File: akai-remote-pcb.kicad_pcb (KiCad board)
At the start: 2 copper layers, 55 x 35 mm, 19 parts, among them J1 Conn_01x11, Q1 T2N7002AK, Q2 T2N7002AK, Q3 T2N7002AK, Q4 T2N7002AK, Q5 T2N7002AK, Q6 T2N7002AK, Q7 T2N7002AK, U1 MOUDLE-SEEEDUINO-XIAO-ESP32C3

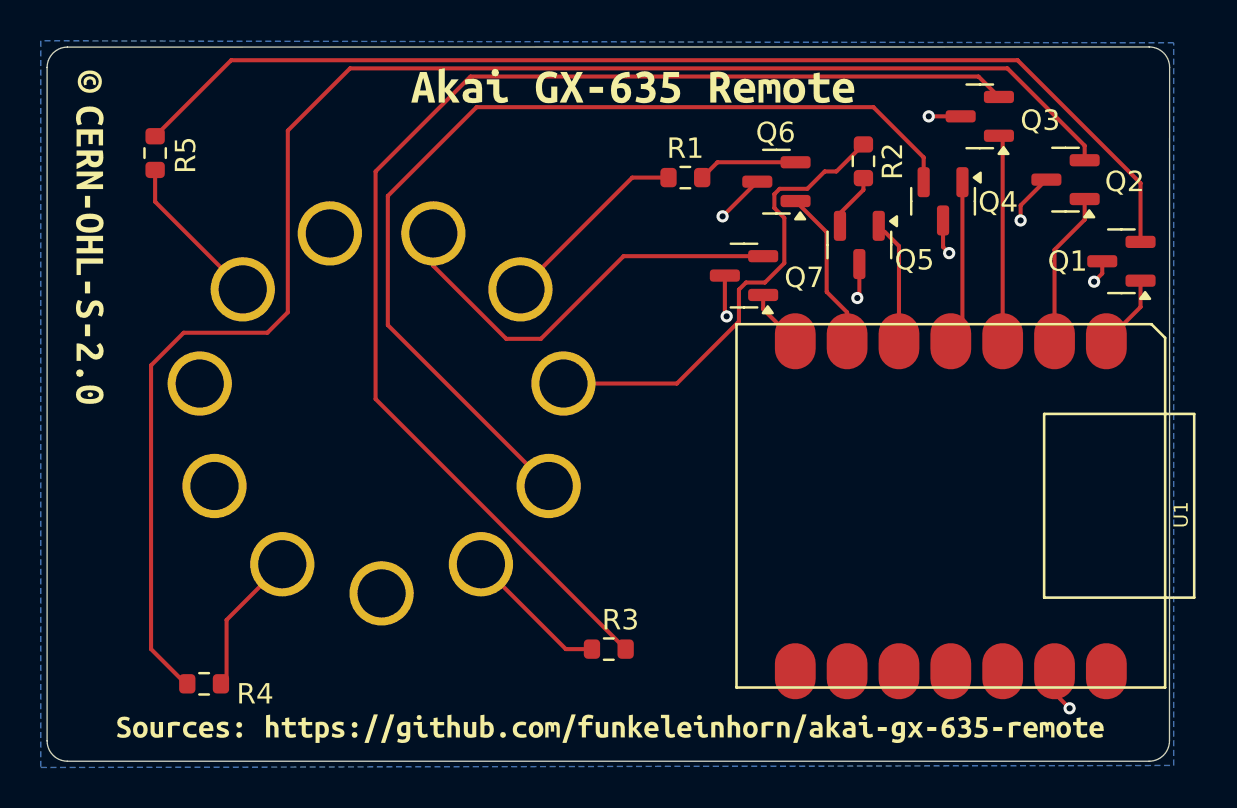
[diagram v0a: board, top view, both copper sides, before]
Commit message: Fix MOSFET direction and add external pull-down resistors
This commit fixes the direction of the MOSFETs and adds external
pull-down resistors to their gates to prevent undefined behavior when
the ESP is not powered.
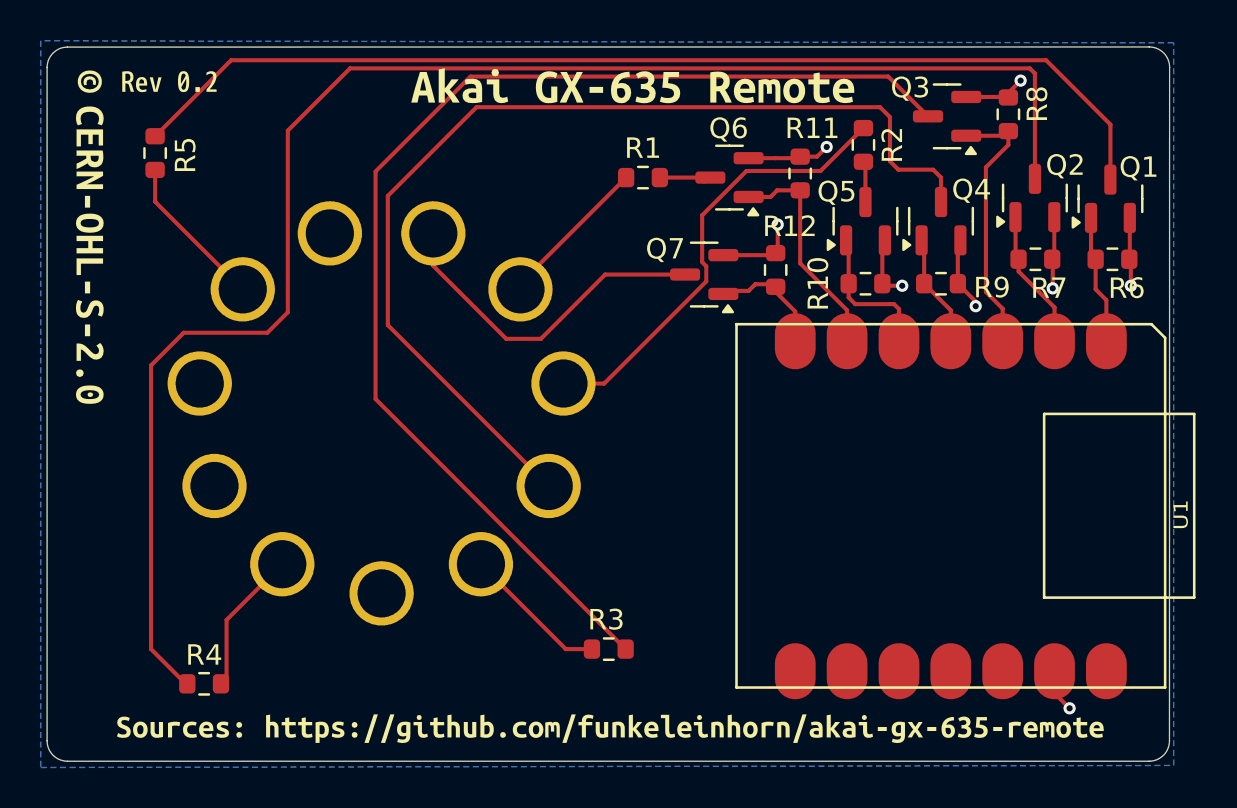
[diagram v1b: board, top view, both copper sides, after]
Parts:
- added R10: 100K, Resistor_SMD:R_0603_1608Metric, F.Cu at (162.3, 90.1)
- added R11: 100K, Resistor_SMD:R_0603_1608Metric, F.Cu at (159.1, 84.7)
- added R12: 100K, Resistor_SMD:R_0603_1608Metric, F.Cu at (157.9, 89.4)
- added R6: 100K, Resistor_SMD:R_0603_1608Metric, F.Cu at (174.4, 88.9)
- added R7: 100K, Resistor_SMD:R_0603_1608Metric, F.Cu at (170.6, 88.9)
- added R8: 100K, Resistor_SMD:R_0603_1608Metric, F.Cu at (169.3, 81.8)
- added R9: 100K, Resistor_SMD:R_0603_1608Metric, F.Cu at (166.0, 90.1)
- added kibuzzard-68C59956: G***, kibuzzard-68C59956, F.Cu at (128.2, 80.2)
- moved Q1 3.11 mm to (174.3, 85.9), turned to 90 degrees
- moved Q6 2.31 mm to (155.6, 84.9)
- moved R1 2.07 mm to (151.4, 84.9)
- moved Q7 1.95 mm to (154.4, 89.7)
- moved Q2 1.75 mm to (170.6, 85.9), turned to 90 degrees
- moved Q3 1.60 mm to (166.3, 81.9)
- moved Q5 1.20 mm to (162.3, 87.0), turned to 90 degrees
- moved Q4 0.98 mm to (166.0, 87.0), turned to 90 degrees
- moved R2 0.80 mm to (162.2, 83.3)
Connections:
- Q1 pad 2: Net-(Q1-S) -> GND
- Q1 pad 3: GND -> Net-(Q1-D)
- Q2 pad 2: Net-(Q2-S) -> GND
- Q2 pad 3: GND -> Net-(Q2-D)
- Q3 pad 2: Net-(Q3-S) -> GND
- Q3 pad 3: GND -> Net-(Q3-D)
- Q4 pad 2: /RWD -> GND
- Q4 pad 3: GND -> /RWD
- Q5 pad 2: Net-(Q5-S) -> GND
- Q5 pad 3: GND -> Net-(Q5-D)
- Q6 pad 2: Net-(Q6-S) -> GND
- Q6 pad 3: GND -> Net-(Q6-D)
- Q7 pad 2: /FF -> GND
- Q7 pad 3: GND -> /FF
- R1 pad 2: Net-(Q6-S) -> Net-(Q6-D)
- R2 pad 2: Net-(Q5-S) -> Net-(Q5-D)
- R3 pad 2: Net-(Q3-S) -> Net-(Q3-D)
- R4 pad 2: Net-(Q2-S) -> Net-(Q2-D)
- R5 pad 2: Net-(Q1-S) -> Net-(Q1-D)
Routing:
- net Net-(Q2-D): track 0.00 -> 76.2 mm
- net Net-(Q2-S): track 75.6 -> 0.00 mm
- net Net-(Q3-S): track 61.4 -> 0.00 mm
- net Net-(Q3-D): track 0.00 -> 58.3 mm
- net Net-(Q1-S): track 55.2 -> 0.00 mm
- net Net-(Q1-D): track 0.00 -> 52.3 mm
- net GND: track 15.0 -> 27.4 mm
- net Net-(Q6-S): track 4.89 -> 0.00 mm
- net /FF: track 20.9 -> 16.7 mm
- net Net-(Q6-G): track 7.91 -> 11.0 mm
- net Net-(Q7-G): track 2.92 -> 5.89 mm
- net Net-(Q3-G): track 10.3 -> 13.2 mm
- net Net-(Q5-S): track 2.81 -> 0.00 mm
- net Net-(Q1-G): track 3.66 -> 6.35 mm
- net Net-(Q6-D): track 0.00 -> 2.62 mm
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
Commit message: Fix remote connector pinout, rework routing for cleaner design
This commit fixes the pinout of the Akai GX 635 remote connector
which was wrong in older revisions. To allow for cleaner routing
the wiring of remote connector pins to the MOSFETs was changed.
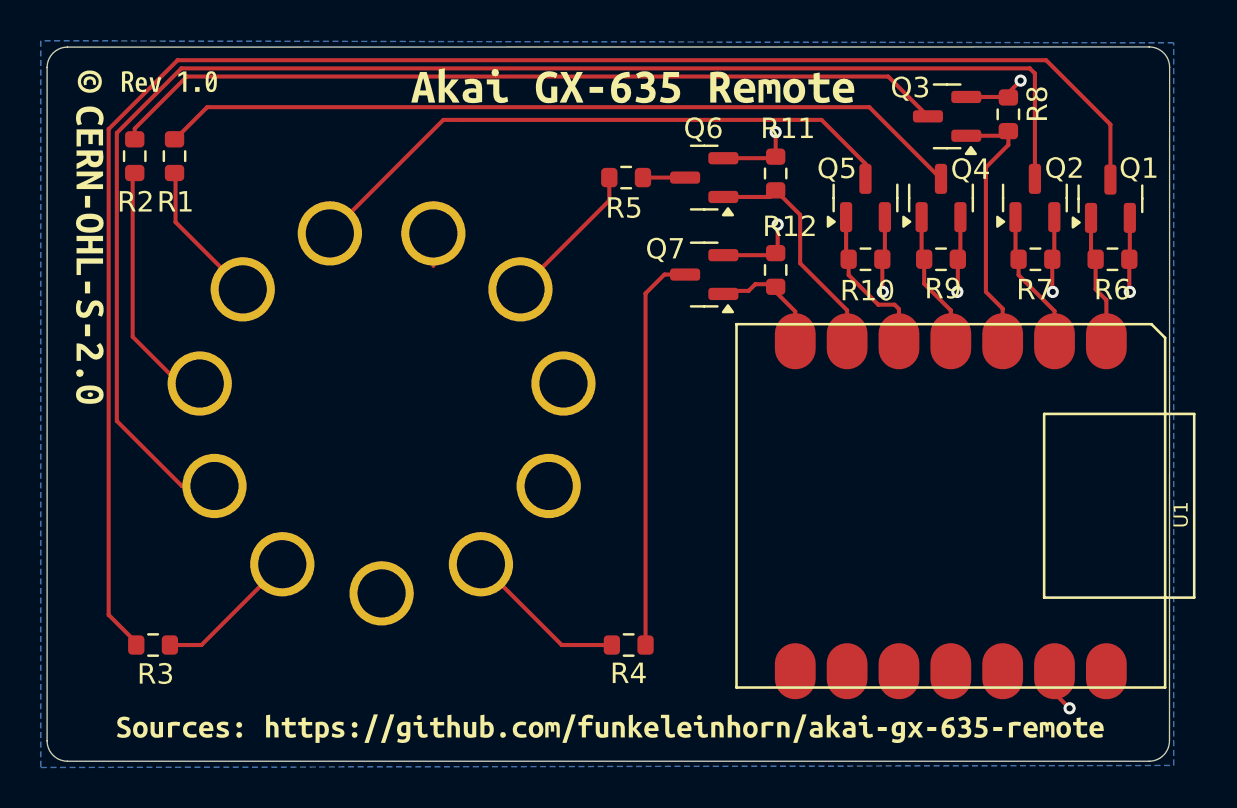
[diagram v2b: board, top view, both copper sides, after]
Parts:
- removed kibuzzard-68C59956: G***, kibuzzard-68C59956
- added kibuzzard-68D13955: G***, kibuzzard-68D13955, F.Cu at (128.2, 80.2)
- moved R2 35.7 mm to (126.5, 83.8), turned to 90 degrees
- moved R5 23.1 mm to (150.6, 84.9), turned to 0 degrees
- moved R1 23.0 mm to (128.4, 83.8), turned to 90 degrees
- moved R3 22.3 mm to (127.4, 107.8), turned to 180 degrees
- moved R4 20.9 mm to (150.7, 107.8), turned to 0 degrees
- moved Q6 1.24 mm to (154.4, 84.9)
- moved R10 1.20 mm to (162.3, 88.9)
- moved R11 1.20 mm to (157.9, 84.7)
- moved R9 1.20 mm to (166.0, 88.9)
- moved Q4 1.14 mm to (166.0, 85.9)
- moved Q5 1.14 mm to (162.3, 85.9)
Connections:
- J1 pad 1: /FF -> unconnected-(J1-Pin_1-Pad1)
- J1 pad 10: /PAUSE -> /FWD
- J1 pad 11: unconnected-(J1-Pin_11-Pad11) -> /FF
- J1 pad 2: /FWD -> /PAUSE
- J1 pad 3: /REV -> unconnected-(J1-Pin_3-Pad3)
- J1 pad 4: /RWD -> GND
- J1 pad 5: /STOP -> /REC
- J1 pad 7: /REC -> /STOP
- J1 pad 8: GND -> /RWD
- J1 pad 9: unconnected-(J1-Pin_9-Pad9) -> /REV
- Q2 pad 3: Net-(Q2-D) -> /RWD
- Q4 pad 3: /RWD -> Net-(Q4-D)
- Q5 pad 3: Net-(Q5-D) -> /FF
- Q7 pad 3: /FF -> Net-(Q7-D)
- R1 pad 2: Net-(Q6-D) -> Net-(Q4-D)
- R2 pad 2: Net-(Q5-D) -> Net-(Q3-D)
- R3 pad 2: Net-(Q3-D) -> Net-(Q1-D)
- R4 pad 2: Net-(Q2-D) -> Net-(Q7-D)
- R5 pad 2: Net-(Q1-D) -> Net-(Q6-D)
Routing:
- net Net-(Q2-D): track 76.2 -> 0.00 mm
- net Net-(Q4-D): track 0.00 -> 39.7 mm
- net Net-(Q1-D): track 52.3 -> 80.3 mm
- net /RWD: track 50.3 -> 71.8 mm
- net Net-(Q7-D): track 0.00 -> 19.5 mm
- net Net-(Q3-D): track 58.3 -> 41.3 mm
- net /FF: track 16.7 -> 30.2 mm
- net /REV: track 22.1 -> 11.9 mm
- net Net-(Q5-D): track 2.02 -> 0.00 mm
- net unconnected-(J1-Pin_1-Pad1): track 0.00 -> 1.60 mm
- net Net-(Q4-G): track 6.34 -> 7.48 mm
- net Net-(Q6-G): track 11.0 -> 12.0 mm
- net /REC: track 7.06 -> 8.05 mm
- net GND: track 27.4 -> 28.4 mm
- net /FWD: track 7.92 -> 7.32 mm
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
